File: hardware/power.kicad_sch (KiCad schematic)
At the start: 35 parts, among them U23 TPS54302, U29 TPS7A4701, U3 TPS7A7002DDA, U30 TPS7A7002DDA, U32 TPS7A4701

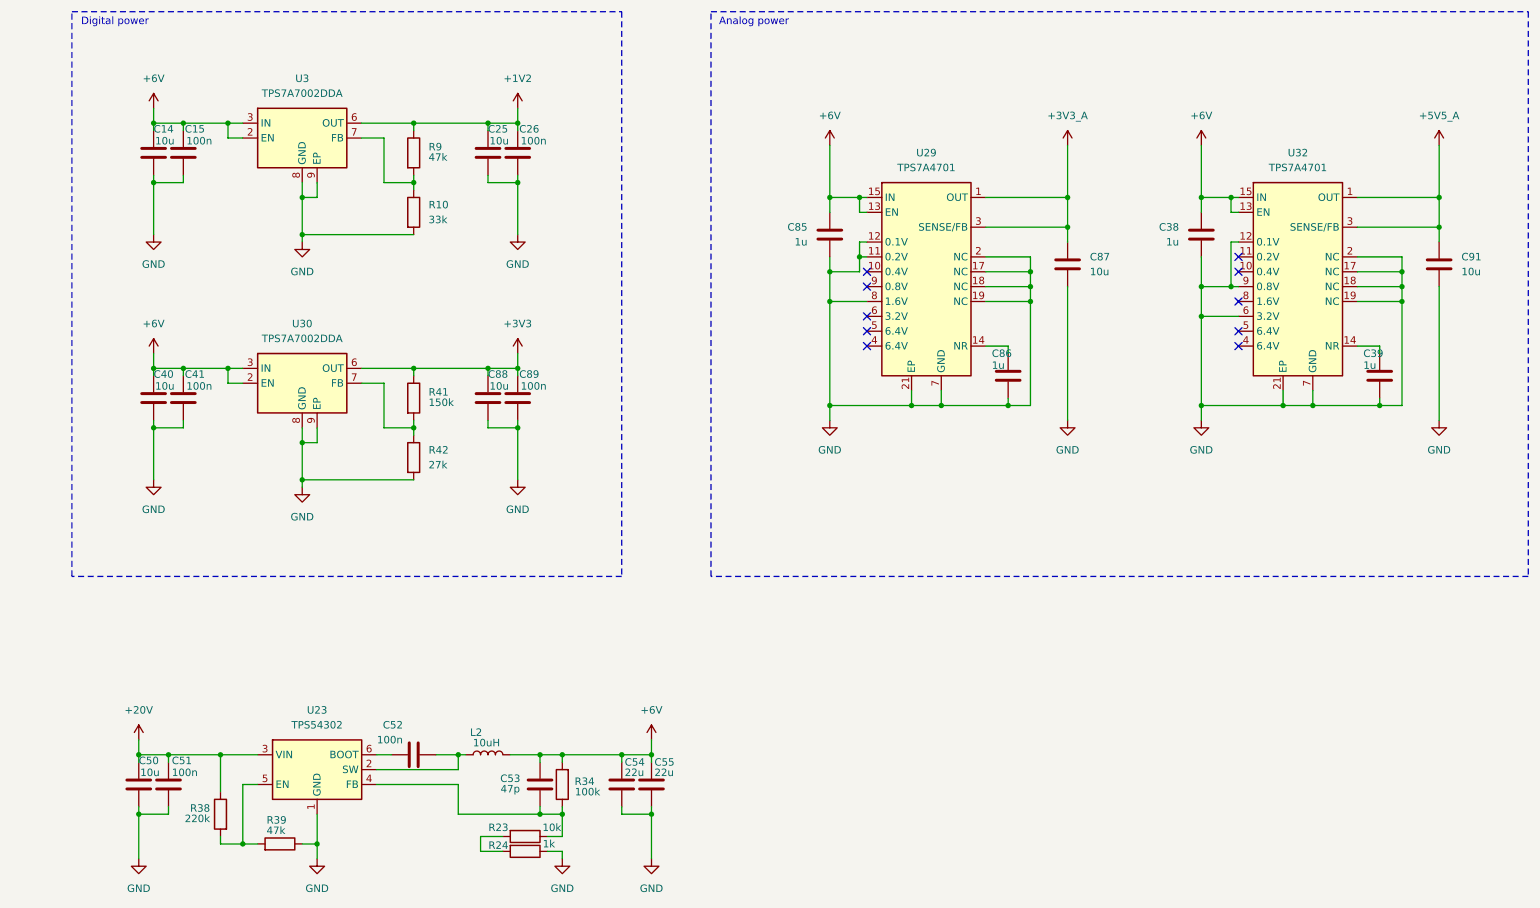
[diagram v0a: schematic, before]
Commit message: complete schematic wiring
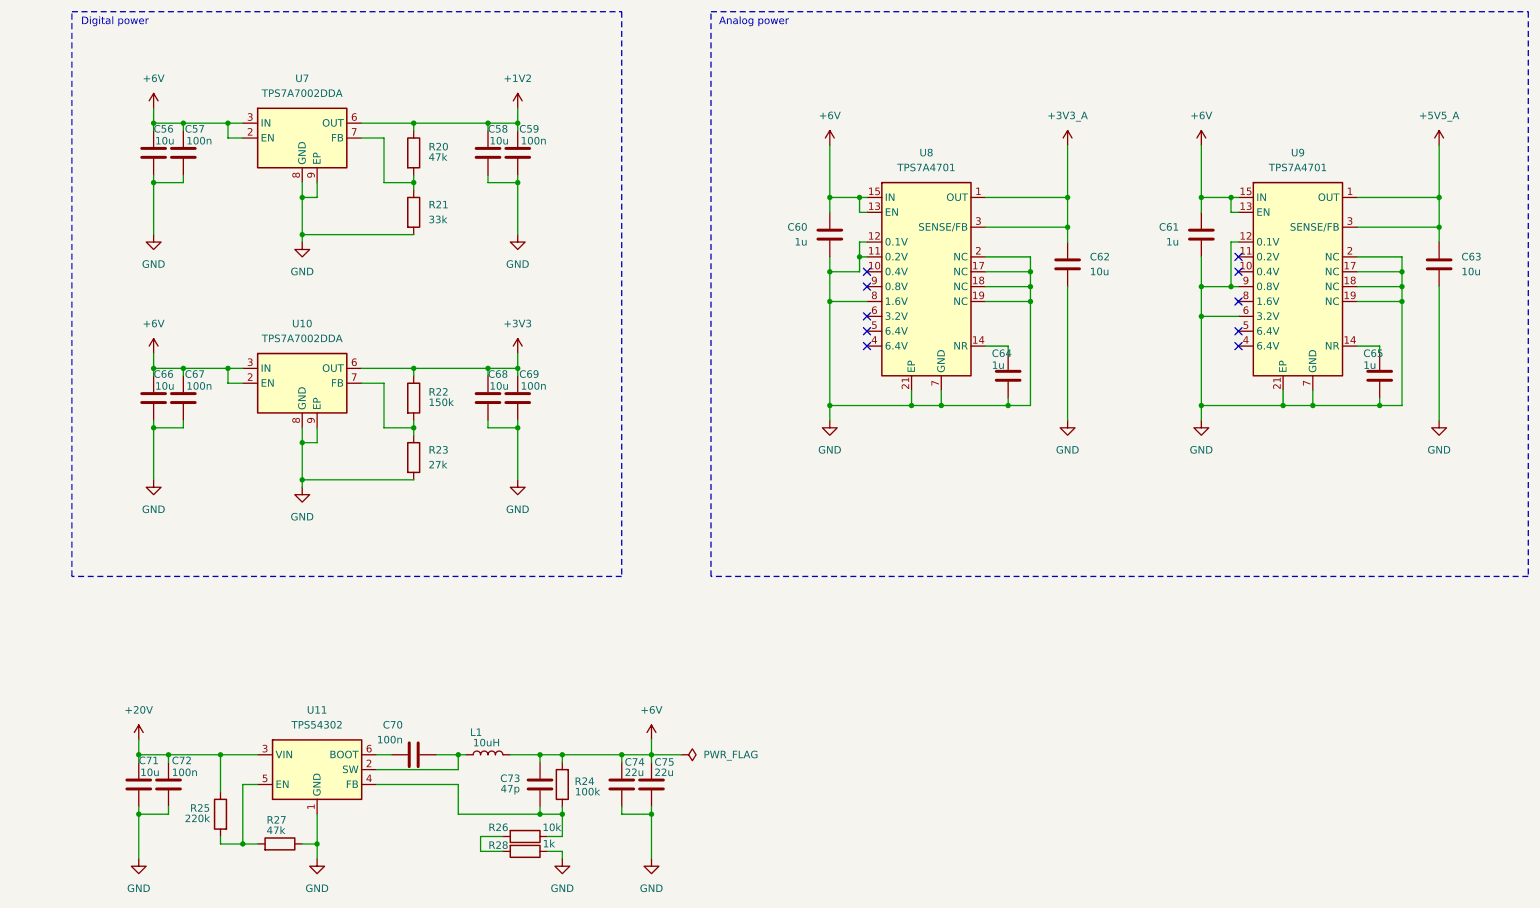
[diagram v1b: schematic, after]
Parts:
- renumbered C14 to C56, C15 to C57, C25 to C58, C26 to C59, C85 to C60, C38 to C61, C87 to C62, C91 to C63, C86 to C64, C39 to C65, C40 to C66, C41 to C67, C88 to C68, C89 to C69, C52 to C70, C50 to C71, C51 to C72, C53 to C73, C54 to C74, C55 to C75, L2 to L1, R9 to R20, R10 to R21, R41 to R22, R42 to R23, R34 to R24, R38 to R25, R23 to R26, R39 to R27, R24 to R28, U30 to U10, U23 to U11, U3 to U7, U29 to U8, U32 to U9

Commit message: update power system + add LCSC part numbers
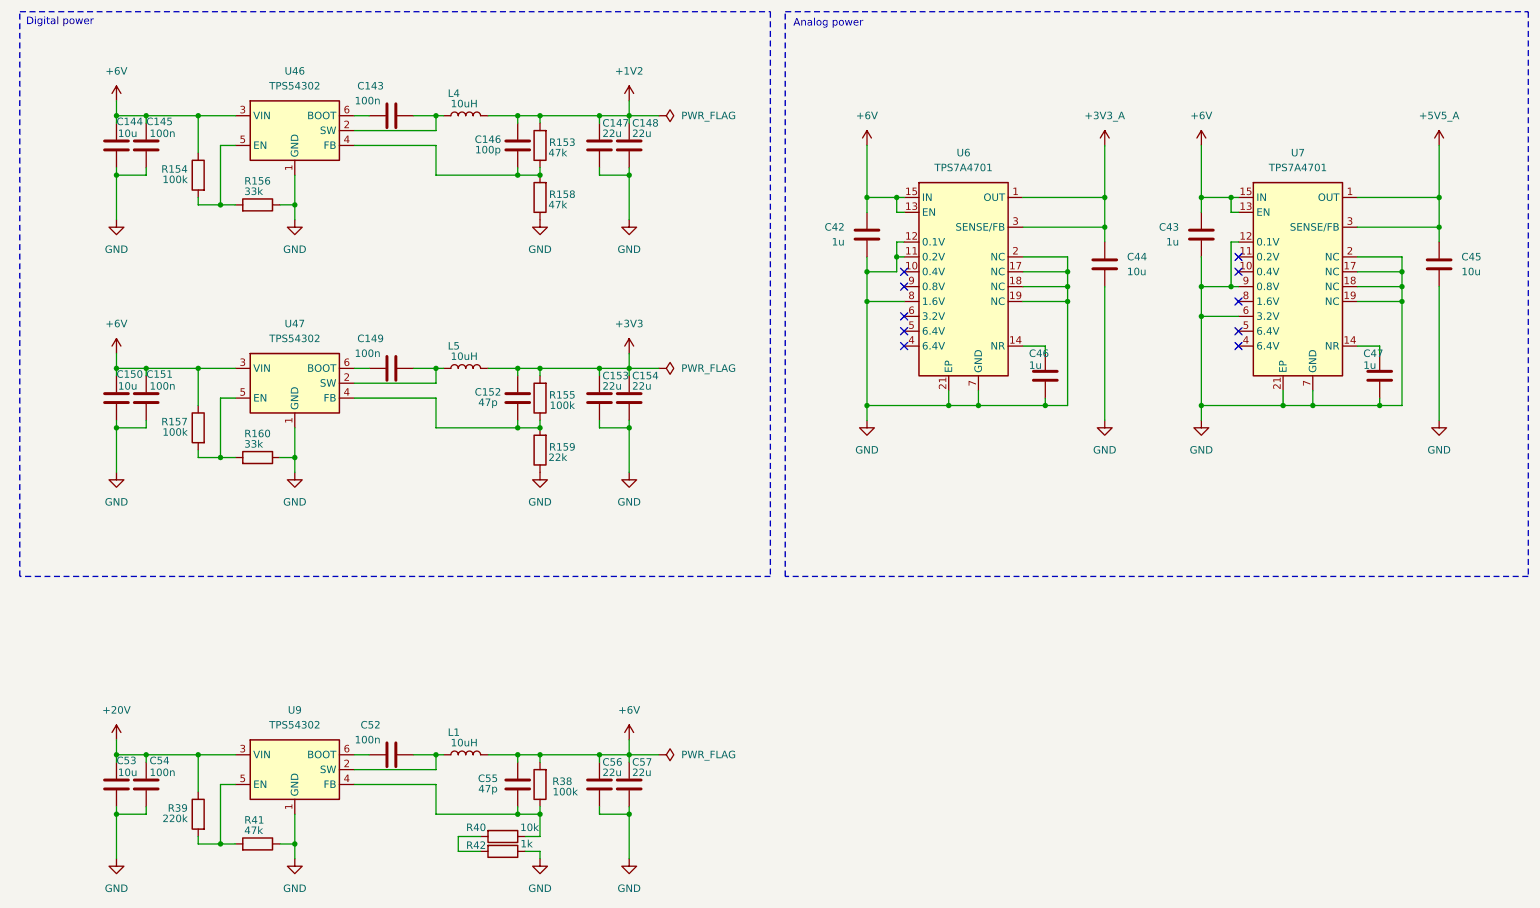
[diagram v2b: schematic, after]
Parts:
- removed C56, C58, C66, C68: 10u, Capacitor_SMD:C_1206_3216Metric, symbol Device:C
- removed C57, C59, C67, C69: 100n, symbol Device:C
- removed R20: 47k, symbol Device:R
- removed R21: 33k, symbol Device:R
- removed R22: 150k, symbol Device:R
- removed R23: 27k, symbol Device:R
- removed U10, U7: TPS7A7002DDA, Package_SO:TI_SO-PowerPAD-8, symbol Regulator_Linear:TPS7A7001DDA
- added C143, C145, C149, C151: 100n, Capacitor_SMD:C_0402_1005Metric, symbol Device:C
- added C144, C150: 10u, Capacitor_SMD:C_1206_3216Metric, symbol Device:C
- added C146: 100p, Capacitor_SMD:C_0402_1005Metric, symbol Device:C
- added C147, C148, C153, C154: 22u, Capacitor_SMD:C_0603_1608Metric, symbol Device:C
- added C152: 47p, Capacitor_SMD:C_0402_1005Metric, symbol Device:C
- added L4, L5: 10uH, Inductor_SMD:L_Changjiang_FXL0630, symbol Device:L
- added R153, R158: 47k, Resistor_SMD:R_0402_1005Metric, symbol Device:R
- added R154, R157: 100k, Resistor_SMD:R_0603_1608Metric, symbol Device:R
- added R155: 100k, Resistor_SMD:R_0402_1005Metric, symbol Device:R
- added R156, R160: 33k, Resistor_SMD:R_0402_1005Metric, symbol Device:R
- added R159: 22k, Resistor_SMD:R_0402_1005Metric, symbol Device:R
- added U46, U47: TPS54302, Package_TO_SOT_SMD:SOT-23-6, symbol Regulator_Switching:TPS54302
- C42: renamed from C60; footprint Capacitor_SMD:C_0603_1608Metric -> Capacitor_SMD:C_0805_2012Metric; LCSC C15849 -> C28323
- C43: renamed from C61; footprint Capacitor_SMD:C_0603_1608Metric -> Capacitor_SMD:C_0805_2012Metric; LCSC C15849 -> C28323
- C46: renamed from C64; footprint Capacitor_SMD:C_0603_1608Metric -> Capacitor_SMD:C_0805_2012Metric; LCSC C15849 -> C28323
- C47: renamed from C65; footprint Capacitor_SMD:C_0603_1608Metric -> Capacitor_SMD:C_0805_2012Metric; LCSC C15849 -> C28323
- L1: footprint Inductor_SMD:L_Changjiang_FXL0530 -> Inductor_SMD:L_Changjiang_FXL0630; LCSC C177248 -> C167223
- R39: renamed from R25; footprint (none) -> Resistor_SMD:R_0603_1608Metric; LCSC (none) -> C22961
- R40: renamed from R26; LCSC C25768 -> C25744
- R41: renamed from R27; footprint (none) -> Resistor_SMD:R_0402_1005Metric; LCSC (none) -> C25792
- R42: renamed from R28; LCSC C25768 -> C11702
- U9: renamed from U11; LCSC (none) -> C129370
- renumbered C62 to C44, C63 to C45, C70 to C52, C71 to C53, C72 to C54, C73 to C55, C74 to C56, C75 to C57, R24 to R38, U8 to U6, U9 to U7
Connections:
- net +1V2: now also C146.2, C147.2, C148.2, L4.2, R153.2
- net +3V3: now also C152.2, C153.2, C154.2, L5.2, R155.2
- net +6V: now also C144.1, C145.2, C150.1, C151.2, R154.1, R157.1, U46.3 (VIN), U47.3 (VIN)
- net GND: now also C144.2, C145.1, C147.1, C148.1, C150.2, C151.1, C153.1, C154.1, R156.1, R158.1, R159.1, R160.1, U46.1 (GND), U47.1 (GND)
- new net: R157.2, R160.2, U47.5 (EN)
- new net: C143.1, U46.6 (BOOT)
- new net: C143.2, L4.1, U46.2 (SW)
- new net: R154.2, R156.2, U46.5 (EN)
- new net: C146.1, R153.1, R158.2, U46.4 (FB)
- new net: C152.1, R155.1, R159.2, U47.4 (FB)
- new net: C149.2, L5.1, U47.2 (SW)
- new net: C149.1, U47.6 (BOOT)
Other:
- moved on the sheet: C42, C44, C46, C52, C53, C54, C55, C56, C57, L1, R38, R39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

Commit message: apply manufacturing BOM
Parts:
- renumbered C143 to C38, C144 to C39, C145 to C40, C146 to C41, C147 to C42, C148 to C43, C42 to C44, C43 to C45, C44 to C46, C45 to C47, C149 to C48, C46 to C49, C47 to C50, C150 to C51, C151 to C52, C152 to C53, C153 to C54, C154 to C55, C52 to C56, C53 to C57, C54 to C58, C55 to C59, C56 to C60, C57 to C61, L4 to L1, L5 to L2, L1 to L3, R153 to R38, R154 to R39, R158 to R40, R156 to R41, R155 to R42, R157 to R43, R159 to R44, R160 to R45, R38 to R46, R39 to R47, R40 to R48, R41 to R49, R42 to R50, U46 to U5, U47 to U8

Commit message: route
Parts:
- renumbered C38 to C41, C39 to C42, C40 to C43, C41 to C44, C42 to C45, C43 to C46, C44 to C47, C45 to C48, C46 to C49, C47 to C50, C48 to C51, C49 to C52, C50 to C53, C51 to C54, C52 to C55, C53 to C56, C54 to C57, C55 to C58, C56 to C59, C57 to C60, C58 to C61, C59 to C62, C60 to C63, C61 to C64
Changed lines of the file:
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@@
 		(on_board yes)
 		(dnp no)
-		(property "Reference" "C49"
+		(property "Reference" "C52"
 			(at 192.786 86.36 0)
 			(effects
@@
 			(project "digital"
 				(path "/4c5c7ce5-09d6-4a32-b2a0-f32b0c47f27d/679bd25b-959e-4fa5-97a0-e7c13c15ad82"
-					(reference "C49")
+					(reference "C52")
 					(unit 1)
 				)
@@
 		(on_board yes)
 		(dnp no)
-		(property "Reference" "C38"
+		(property "Reference" "C41"
 			(at 80.264 40.64 90)
 			(effects
@@
 			(project "digital"
 				(path "/4c5c7ce5-09d6-4a32-b2a0-f32b0c47f27d/679bd25b-959e-4fa5-97a0-e7c13c15ad82"
-					(reference "C38")
+					(reference "C41")
 					(unit 1)
 				)
@@
 		(on_board yes)
 		(dnp no)
-		(property "Reference" "C40"
+		(property "Reference" "C43"
 			(at 44.196 46.736 0)
 			(effects
@@
 			(project "digital"
 				(path "/4c5c7ce5-09d6-4a32-b2a0-f32b0c47f27d/679bd25b-959e-4fa5-97a0-e7c13c15ad82"
-					(reference "C40")
+					(reference "C43")
 					(unit 1)
 				)
@@
 		(dnp no)
 		(fields_autoplaced yes)
-		(property "Reference" "C45"
+		(property "Reference" "C48"
 			(at 218.44 64.7699 0)
 			(effects
@@
 			(project "digital"
 				(path "/4c5c7ce5-09d6-4a32-b2a0-f32b0c47f27d/679bd25b-959e-4fa5-97a0-e7c13c15ad82"
-					(reference "C45")
+					(reference "C48")
 					(unit 1)
 				)
@@
 		(dnp no)
 		(fields_autoplaced yes)
-		(property "Reference" "C44"
+		(property "Reference" "C47"
 			(at 161.29 64.7699 0)
 			(effects
@@
 			(project "digital"
 				(path "/4c5c7ce5-09d6-4a32-b2a0-f32b0c47f27d/679bd25b-959e-4fa5-97a0-e7c13c15ad82"
-					(reference "C44")
+					(reference "C47")
 					(unit 1)
 				)
@@
 		(on_board yes)
 		(dnp no)
-		(property "Reference" "C51"
+		(property "Reference" "C54"
 			(at 36.83 89.916 0)
 			(effects
@@
 			(project "digital"
 				(path "/4c5c7ce5-09d6-4a32-b2a0-f32b0c47f27d/679bd25b-959e-4fa5-97a0-e7c13c15ad82"
-					(reference "C51")
+					(reference "C54")
 					(unit 1)
 				)
@@
 		(on_board yes)
 		(dnp no)
-		(property "Reference" "C50"
+		(property "Reference" "C53"
 			(at 249.936 86.36 0)
 			(effects
@@
 			(project "digital"
 				(path "/4c5c7ce5-09d6-4a32-b2a0-f32b0c47f27d/679bd25b-959e-4fa5-97a0-e7c13c15ad82"
-					(reference "C50")
+					(reference "C53")
 					(unit 1)
 				)
@@
 		(on_board yes)
 		(dnp no)
-		(property "Reference" "C56"
+		(property "Reference" "C59"
 			(at 80.264 149.86 90)
 			(effects
@@
 			(project "digital"
 				(path "/4c5c7ce5-09d6-4a32-b2a0-f32b0c47f27d/679bd25b-959e-4fa5-97a0-e7c13c15ad82"
-					(reference "C56")
+					(reference "C59")
 					(unit 1)
 				)
@@
 		(on_board yes)
 		(dnp no)
-		(property "Reference" "C42"
+		(property "Reference" "C45"
 			(at 119.888 46.99 0)
 			(effects
@@
 			(project "digital"
 				(path "/4c5c7ce5-09d6-4a32-b2a0-f32b0c47f27d/679bd25b-959e-4fa5-97a0-e7c13c15ad82"
-					(reference "C42")
+					(reference "C45")
 					(unit 1)
 				)
@@
 		(on_board yes)
 		(dnp no)
-		(property "Reference" "C41"
+		(property "Reference" "C44"
 			(at 100.33 49.784 0)
 			(effects
@@
 			(project "digital"
 				(path "/4c5c7ce5-09d6-4a32-b2a0-f32b0c47f27d/679bd25b-959e-4fa5-97a0-e7c13c15ad82"
-					(reference "C41")
+					(reference "C44")
 					(unit 1)
 				)
@@
 		(on_board yes)
 		(dnp no)
-		(property "Reference" "C59"
+		(property "Reference" "C62"
 			(at 100.33 159.004 0)
 			(effects
@@
 			(project "digital"
 				(path "/4c5c7ce5-09d6-4a32-b2a0-f32b0c47f27d/679bd25b-959e-4fa5-97a0-e7c13c15ad82"
-					(reference "C59")
+					(reference "C62")
 					(unit 1)
 				)
@@
 		(on_board yes)
 		(dnp no)
-		(property "Reference" "C52"
+		(property "Reference" "C55"
 			(at 44.196 89.916 0)
 			(effects
@@
 			(project "digital"
 				(path "/4c5c7ce5-09d6-4a32-b2a0-f32b0c47f27d/679bd25b-959e-4fa5-97a0-e7c13c15ad82"
-					(reference "C52")
+					(reference "C55")
 					(unit 1)
 				)
@@
 		(on_board yes)
 		(dnp no)
-		(property "Reference" "C57"
+		(property "Reference" "C60"
 			(at 36.83 155.956 0)
 			(effects
@@
 			(project "digital"
 				(path "/4c5c7ce5-09d6-4a32-b2a0-f32b0c47f27d/679bd25b-959e-4fa5-97a0-e7c13c15ad82"
-					(reference "C57")
+					(reference "C60")
 					(unit 1)
 				)
@@
 		(on_board yes)
 		(dnp no)
-		(property "Reference" "C53"
+		(property "Reference" "C56"
 			(at 100.33 92.964 0)
 			(effects
@@
 			(project "digital"
 				(path "/4c5c7ce5-09d6-4a32-b2a0-f32b0c47f27d/679bd25b-959e-4fa5-97a0-e7c13c15ad82"
-					(reference "C53")
+					(reference "C56")
 					(unit 1)
 				)
@@
 		(on_board yes)
 		(dnp no)
-		(property "Reference" "C43"
+		(property "Reference" "C46"
 			(at 124.968 46.99 0)
 			(effects
@@
 			(project "digital"
 				(path "/4c5c7ce5-09d6-4a32-b2a0-f32b0c47f27d/679bd25b-959e-4fa5-97a0-e7c13c15ad82"
-					(reference "C43")
+					(reference "C46")
 					(unit 1)
 				)
@@
 		(on_board yes)
 		(dnp no)
-		(property "Reference" "C60"
+		(property "Reference" "C63"
 			(at 119.888 156.21 0)
 			(effects
@@
 			(project "digital"
 				(path "/4c5c7ce5-09d6-4a32-b2a0-f32b0c47f27d/679bd25b-959e-4fa5-97a0-e7c13c15ad82"
-					(reference "C60")
+					(reference "C63")
 					(unit 1)
 				)
@@
 		(dnp no)
 		(fields_autoplaced yes)
-		(property "Reference" "C46"
+		(property "Reference" "C49"
 			(at 209.55 69.8499 0)
 			(effects
@@
 			(project "digital"
 				(path "/4c5c7ce5-09d6-4a32-b2a0-f32b0c47f27d/679bd25b-959e-4fa5-97a0-e7c13c15ad82"
-					(reference "C46")
+					(reference "C49")
 					(unit 1)
 				)
@@
 		(on_board yes)
 		(dnp no)
-		(property "Reference" "C54"
+		(property "Reference" "C57"
 			(at 119.888 90.17 0)
 			(effects
@@
 			(project "digital"
 				(path "/4c5c7ce5-09d6-4a32-b2a0-f32b0c47f27d/679bd25b-959e-4fa5-97a0-e7c13c15ad82"
-					(reference "C54")
+					(reference "C57")
 					(unit 1)
 				)
@@
 		(on_board yes)
 		(dnp no)
-		(property "Reference" "C55"
+		(property "Reference" "C58"
 			(at 124.968 90.17 0)
 			(effects
@@
 			(project "digital"
 				(path "/4c5c7ce5-09d6-4a32-b2a0-f32b0c47f27d/679bd25b-959e-4fa5-97a0-e7c13c15ad82"
-					(reference "C55")
+					(reference "C58")
 					(unit 1)
 				)
@@
 		(on_board yes)
 		(dnp no)
-		(property "Reference" "C39"
+		(property "Reference" "C42"
 			(at 36.83 46.736 0)
 			(effects
@@
 			(project "digital"
 				(path "/4c5c7ce5-09d6-4a32-b2a0-f32b0c47f27d/679bd25b-959e-4fa5-97a0-e7c13c15ad82"
-					(reference "C39")
+					(reference "C42")
 					(unit 1)
 				)
@@
 		(on_board yes)
 		(dnp no)
-		(property "Reference" "C61"
+		(property "Reference" "C64"
 			(at 124.968 156.21 0)
 			(effects
@@
 			(project "digital"
 				(path "/4c5c7ce5-09d6-4a32-b2a0-f32b0c47f27d/679bd25b-959e-4fa5-97a0-e7c13c15ad82"
-					(reference "C61")
+					(reference "C64")
 					(unit 1)
 				)
@@
 		(dnp no)
 		(fields_autoplaced yes)
-		(property "Reference" "C47"
+		(property "Reference" "C50"
 			(at 266.7 69.8499 0)
 			(effects
@@
 			(project "digital"
 				(path "/4c5c7ce5-09d6-4a32-b2a0-f32b0c47f27d/679bd25b-959e-4fa5-97a0-e7c13c15ad82"
-					(reference "C47")
+					(reference "C50")
 					(unit 1)
 				)
@@
 		(on_board yes)
 		(dnp no)
-		(property "Reference" "C48"
+		(property "Reference" "C51"
 			(at 80.264 83.82 90)
 			(effects
@@
 			(project "digital"
 				(path "/4c5c7ce5-09d6-4a32-b2a0-f32b0c47f27d/679bd25b-959e-4fa5-97a0-e7c13c15ad82"
-					(reference "C48")
+					(reference "C51")
 					(unit 1)
 				)
@@
 		(on_board yes)
 		(dnp no)
-		(property "Reference" "C58"
+		(property "Reference" "C61"
 			(at 44.196 155.956 0)
 			(effects
@@
 			(project "digital"
 				(path "/4c5c7ce5-09d6-4a32-b2a0-f32b0c47f27d/679bd25b-959e-4fa5-97a0-e7c13c15ad82"
-					(reference "C58")
+					(reference "C61")
 					(unit 1)
 				)

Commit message: fabrication
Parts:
- C44: LCSC C1567 -> C1546
- C45, C46, C57, C58, C63, C64: LCSC C59461 -> C60077
- R39, R43: LCSC C22961 -> C25803
- R41, R45: LCSC C25792 -> C25779
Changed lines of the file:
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@@
 			)
 		)
-		(property "LCSC" "C22961"
+		(property "LCSC" "C25803"
 			(at 50.8 99.06 0)
 			(effects
@@
 			)
 		)
-		(property "LCSC" "C25792"
+		(property "LCSC" "C25779"
 			(at 60.96 60.96 90)
 			(effects
@@
 			)
 		)
-		(property "LCSC" "C59461"
+		(property "LCSC" "C60077"
 			(at 119.38 50.8 0)
 			(effects
@@
 			)
 		)
-		(property "LCSC" "C1567"
+		(property "LCSC" "C1546"
 			(at 105.41 50.8 0)
 			(effects
@@
 			)
 		)
-		(property "LCSC" "C25792"
+		(property "LCSC" "C25779"
 			(at 60.96 104.14 90)
 			(effects
@@
 			)
 		)
-		(property "LCSC" "C22961"
+		(property "LCSC" "C25803"
 			(at 50.8 55.88 0)
 			(effects
@@
 			)
 		)
-		(property "LCSC" "C59461"
+		(property "LCSC" "C60077"
 			(at 124.46 50.8 0)
 			(effects
@@
 			)
 		)
-		(property "LCSC" "C59461"
+		(property "LCSC" "C60077"
 			(at 119.38 160.02 0)
 			(effects
@@
 			)
 		)
-		(property "LCSC" "C59461"
+		(property "LCSC" "C60077"
 			(at 119.38 93.98 0)
 			(effects
@@
 			)
 		)
-		(property "LCSC" "C59461"
+		(property "LCSC" "C60077"
 			(at 124.46 93.98 0)
 			(effects
@@
 			)
 		)
-		(property "LCSC" "C59461"
+		(property "LCSC" "C60077"
 			(at 124.46 160.02 0)
 			(effects
